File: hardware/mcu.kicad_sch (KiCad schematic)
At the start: 55 parts, among them J10 PRPC001DAAN-RC, J11 PRPC006SAAN-RC, J12 PRPC004SAAN-RC, J8 SBH11-NBPC-D05-SM-BK, J9 PRPC006SAAN-RC, U5 AT25SF081B-SSHD-B, U6 MCP9808, U7 STM32L552CETx, Y1 ABS05-32.768KHZ-9-T, Y2 ECS-160-9-37-CKM-TR3

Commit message: HW: Layout power section
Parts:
- C10, C15, C17, C20: Digi-Key Part Number 732-7902-1-ND -> 732-7623-1-ND; Manufacturer Part Number 885012106005 -> 885012107013
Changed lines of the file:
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@@
 			)
 		)
-		(property "Manufacturer Part Number" "885012106005"
+		(property "Manufacturer Part Number" "885012107013"
 			(at 162.56 33.02 0)
 			(effects
@@
 			)
 		)
-		(property "Digi-Key Part Number" "732-7902-1-ND"
+		(property "Digi-Key Part Number" "732-7623-1-ND"
 			(at 162.56 33.02 0)
 			(effects
@@
 			)
 		)
-		(property "Manufacturer Part Number" "885012106005"
+		(property "Manufacturer Part Number" "885012107013"
 			(at 114.3 166.37 0)
 			(effects
@@
 			)
 		)
-		(property "Digi-Key Part Number" "732-7902-1-ND"
+		(property "Digi-Key Part Number" "732-7623-1-ND"
 			(at 114.3 166.37 0)
 			(effects
@@
 			)
 		)
-		(property "Manufacturer Part Number" "885012106005"
+		(property "Manufacturer Part Number" "885012107013"
 			(at 99.06 33.02 0)
 			(effects
@@
 			)
 		)
-		(property "Digi-Key Part Number" "732-7902-1-ND"
+		(property "Digi-Key Part Number" "732-7623-1-ND"
 			(at 99.06 33.02 0)
 			(effects
@@
 			)
 		)
-		(property "Manufacturer Part Number" "885012106005"
+		(property "Manufacturer Part Number" "885012107013"
 			(at 60.96 168.91 0)
 			(effects
@@
 			)
 		)
-		(property "Digi-Key Part Number" "732-7902-1-ND"
+		(property "Digi-Key Part Number" "732-7623-1-ND"
 			(at 60.96 168.91 0)
 			(effects

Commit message: HW: Layout MCU section
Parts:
- TVS10, TVS11, TVS2, TVS3, TVS4, TVS5, TVS6, TVS7, TVS8, TVS9: value SMAJ6.0CA-13-F -> CPDUC5V0USP-HF; footprint Diode_SMD:D_SMA_Handsoldering -> Diode_SMD:D_0603_1608Metric_Pad1.05x0.95mm_HandSolder; Digi-Key Part Number SMAJ6.0CA-13-FDICT-ND -> 641-1765-1-ND; Manufacturer Diodes Incorporated -> Comchip Technology; Manufacturer Part Number SMAJ6.0CA-13-F -> CPDUC5V0USP-HF
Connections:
- net COM_UART_RX: now also J9.4 (Pin_4), TVS5.1 (K); no longer J9.5 (Pin_5), TVS2.1 (K)
- net COM_UART_TX: now also J9.5 (Pin_5), TVS2.1 (K); no longer J9.4 (Pin_4), TVS5.1 (K)
- net I2C_SCL: now also J12.3 (Pin_3), TVS4.1 (K); no longer J12.2 (Pin_2), TVS7.1 (K)
- net I2C_SDA: now also J12.2 (Pin_2), TVS7.1 (K); no longer J12.3 (Pin_3), TVS4.1 (K)
- net MODEM_RX: now also J11.4 (Pin_4), TVS6.1 (K); no longer J11.5 (Pin_5), TVS3.1 (K)
- net MODEM_TX: now also J11.5 (Pin_5), TVS3.1 (K); no longer J11.4 (Pin_4), TVS6.1 (K)
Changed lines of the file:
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@@
 	(wire
 		(pts
-			(xy 271.78 59.69) (xy 271.78 58.42)
-		)
-		(stroke
-			(width 0)
-			(type default)
-		)
-	)
-	(wire
-		(pts
 			(xy 254 105.41) (xy 262.89 105.41)
 		)
@@
 	(wire
 		(pts
-			(xy 262.89 59.69) (xy 262.89 58.42)
-		)
-		(stroke
-			(width 0)
-			(type default)
-		)
-	)
-	(wire
-		(pts
 			(xy 280.67 31.75) (xy 274.32 31.75)
 		)
@@
 	)
 	(label "I2C_SCL"
-		(at 261.62 120.65 180)
+		(at 252.73 123.19 180)
 		(fields_autoplaced yes)
 		(effects
@@
 	)
 	(label "COM_UART_TX"
-		(at 260.35 48.26 180)
+		(at 251.46 50.8 180)
 		(fields_autoplaced yes)
 		(effects
@@
 	)
 	(label "I2C_SDA"
-		(at 252.73 123.19 180)
+		(at 261.62 120.65 180)
 		(fields_autoplaced yes)
 		(effects
@@
 	)
 	(label "COM_UART_RX"
-		(at 251.46 50.8 180)
+		(at 260.35 48.26 180)
 		(fields_autoplaced yes)
 		(effects
@@
 	(hierarchical_label "MODEM_TX"
 		(shape bidirectional)
-		(at 260.35 93.98 180)
+		(at 251.46 96.52 180)
 		(fields_autoplaced yes)
 		(effects
@@
 	(hierarchical_label "MODEM_RX"
 		(shape bidirectional)
-		(at 251.46 96.52 180)
+		(at 260.35 93.98 180)
 		(fields_autoplaced yes)
 		(effects
@@
 			)
 		)
-		(property "Value" "SMAJ6.0CA-13-F"
+		(property "Value" "CPDUC5V0USP-HF"
 			(at 261.62 102.87 90)
 			(effects
@@
 			)
 		)
-		(property "Footprint" "Diode_SMD:D_SMA_Handsoldering"
+		(property "Footprint" "Diode_SMD:D_0603_1608Metric_Pad1.05x0.95mm_HandSolder"
 			(at 271.78 101.6 0)
 			(effects
@@
 			)
 		)
-		(property "Digi-Key Part Number" "SMAJ6.0CA-13-FDICT-ND"
+		(property "Digi-Key Part Number" "641-1765-1-ND"
 			(at 271.78 101.6 0)
 			(effects
@@
 			)
 		)
-		(property "Manufacturer" "Diodes Incorporated"
+		(property "Manufacturer" "Comchip Technology"
 			(at 271.78 101.6 0)
 			(effects
@@
 			)
 		)
-		(property "Manufacturer Part Number" "SMAJ6.0CA-13-F"
+		(property "Manufacturer Part Number" "CPDUC5V0USP-HF"
 			(at 271.78 101.6 0)
 			(effects
@@
 			)
 		)
-		(property "Value" "SMAJ6.0CA-13-F"
+		(property "Value" "CPDUC5V0USP-HF"
 			(at 243.84 102.87 90)
 			(effects
@@
 			)
 		)
-		(property "Footprint" "Diode_SMD:D_SMA_Handsoldering"
+		(property "Footprint" "Diode_SMD:D_0603_1608Metric_Pad1.05x0.95mm_HandSolder"
 			(at 254 101.6 0)
 			(effects
@@
 			)
 		)
-		(property "Digi-Key Part Number" "SMAJ6.0CA-13-FDICT-ND"
+		(property "Digi-Key Part Number" "641-1765-1-ND"
 			(at 254 101.6 0)
 			(effects
@@
 			)
 		)
-		(property "Manufacturer" "Diodes Incorporated"
+		(property "Manufacturer" "Comchip Technology"
 			(at 254 101.6 0)
 			(effects
@@
 			)
 		)
-		(property "Manufacturer Part Number" "SMAJ6.0CA-13-F"
+		(property "Manufacturer Part Number" "CPDUC5V0USP-HF"
 			(at 254 101.6 0)
 			(effects
@@
 			)
 		)
-		(property "Value" "SMAJ6.0CA-13-F"
+		(property "Value" "CPDUC5V0USP-HF"
 			(at 261.62 74.93 90)
 			(effects
@@
 			)
 		)
-		(property "Footprint" "Diode_SMD:D_SMA_Handsoldering"
+		(property "Footprint" "Diode_SMD:D_0603_1608Metric_Pad1.05x0.95mm_HandSolder"
 			(at 271.78 73.66 0)
 			(effects
@@
 			)
 		)
-		(property "Digi-Key Part Number" "SMAJ6.0CA-13-FDICT-ND"
+		(property "Digi-Key Part Number" "641-1765-1-ND"
 			(at 271.78 73.66 0)
 			(effects
@@
 			)
 		)
-		(property "Manufacturer" "Diodes Incorporated"
+		(property "Manufacturer" "Comchip Technology"
 			(at 271.78 73.66 0)
 			(effects
@@
 			)
 		)
-		(property "Manufacturer Part Number" "SMAJ6.0CA-13-F"
+		(property "Manufacturer Part Number" "CPDUC5V0USP-HF"
 			(at 271.78 73.66 0)
 			(effects
@@
 			)
 		)
-		(property "Value" "SMAJ6.0CA-13-F"
+		(property "Value" "CPDUC5V0USP-HF"
 			(at 252.73 102.87 90)
 			(effects
@@
 			)
 		)
-		(property "Footprint" "Diode_SMD:D_SMA_Handsoldering"
+		(property "Footprint" "Diode_SMD:D_0603_1608Metric_Pad1.05x0.95mm_HandSolder"
 			(at 262.89 101.6 0)
 			(effects
@@
 			)
 		)
-		(property "Digi-Key Part Number" "SMAJ6.0CA-13-FDICT-ND"
+		(property "Digi-Key Part Number" "641-1765-1-ND"
 			(at 262.89 101.6 0)
 			(effects
@@
 			)
 		)
-		(property "Manufacturer" "Diodes Incorporated"
+		(property "Manufacturer" "Comchip Technology"
 			(at 262.89 101.6 0)
 			(effects
@@
 			)
 		)
-		(property "Manufacturer Part Number" "SMAJ6.0CA-13-F"
+		(property "Manufacturer Part Number" "CPDUC5V0USP-HF"
 			(at 262.89 101.6 0)
 			(effects
@@
 			)
 		)
-		(property "Value" "SMAJ6.0CA-13-F"
+		(property "Value" "CPDUC5V0USP-HF"
 			(at 252.73 57.15 90)
 			(effects
@@
 			)
 		)
-		(property "Footprint" "Diode_SMD:D_SMA_Handsoldering"
+		(property "Footprint" "Diode_SMD:D_0603_1608Metric_Pad1.05x0.95mm_HandSolder"
 			(at 262.89 55.88 0)
 			(effects
@@
 			)
 		)
-		(property "Digi-Key Part Number" "SMAJ6.0CA-13-FDICT-ND"
+		(property "Digi-Key Part Number" "641-1765-1-ND"
 			(at 262.89 55.88 0)
 			(effects
@@
 			)
 		)
-		(property "Manufacturer" "Diodes Incorporated"
+		(property "Manufacturer" "Comchip Technology"
 			(at 262.89 55.88 0)
 			(effects
@@
 			)
 		)
-		(property "Manufacturer Part Number" "SMAJ6.0CA-13-F"
+		(property "Manufacturer Part Number" "CPDUC5V0USP-HF"
 			(at 262.89 55.88 0)
 			(effects
@@
 			)
 		)
-		(property "Value" "SMAJ6.0CA-13-F"
+		(property "Value" "CPDUC5V0USP-HF"
 			(at 261.62 57.15 90)
 			(effects
@@
 			)
 		)
-		(property "Footprint" "Diode_SMD:D_SMA_Handsoldering"
+		(property "Footprint" "Diode_SMD:D_0603_1608Metric_Pad1.05x0.95mm_HandSolder"
 			(at 271.78 55.88 0)
 			(effects
@@
 			)
 		)
-		(property "Digi-Key Part Number" "SMAJ6.0CA-13-FDICT-ND"
+		(property "Digi-Key Part Number" "641-1765-1-ND"
 			(at 271.78 55.88 0)
 			(effects
@@
 			)
 		)
-		(property "Manufacturer" "Diodes Incorporated"
+		(property "Manufacturer" "Comchip Technology"
 			(at 271.78 55.88 0)
 			(effects
@@
 			)
 		)
-		(property "Manufacturer Part Number" "SMAJ6.0CA-13-F"
+		(property "Manufacturer Part Number" "CPDUC5V0USP-HF"
 			(at 271.78 55.88 0)
 			(effects
@@
 			)
 		)
-		(property "Value" "SMAJ6.0CA-13-F"
+		(property "Value" "CPDUC5V0USP-HF"
 			(at 243.84 129.54 90)
 			(effects
@@
 			)
 		)
-		(property "Footprint" "Diode_SMD:D_SMA_Handsoldering"
+		(property "Footprint" "Diode_SMD:D_0603_1608Metric_Pad1.05x0.95mm_HandSolder"
 			(at 254 128.27 0)
 			(effects
@@
 			)
 		)
-		(property "Digi-Key Part Number" "SMAJ6.0CA-13-FDICT-ND"
+		(property "Digi-Key Part Number" "641-1765-1-ND"
 			(at 254 128.27 0)
 			(effects
@@
 			)
 		)
-		(property "Manufacturer" "Diodes Incorporated"
+		(property "Manufacturer" "Comchip Technology"
 			(at 254 128.27 0)
 			(effects
@@
 			)
 		)
-		(property "Manufacturer Part Number" "SMAJ6.0CA-13-F"
+		(property "Manufacturer Part Number" "CPDUC5V0USP-HF"
 			(at 254 128.27 0)
 			(effects
@@
 			)
 		)
-		(property "Value" "SMAJ6.0CA-13-F"
+		(property "Value" "CPDUC5V0USP-HF"
 			(at 243.84 57.15 90)
 			(effects
@@
 			)
 		)
-		(property "Footprint" "Diode_SMD:D_SMA_Handsoldering"
+		(property "Footprint" "Diode_SMD:D_0603_1608Metric_Pad1.05x0.95mm_HandSolder"
 			(at 254 55.88 0)
 			(effects
@@
 			)
 		)
-		(property "Digi-Key Part Number" "SMAJ6.0CA-13-FDICT-ND"
+		(property "Digi-Key Part Number" "641-1765-1-ND"
 			(at 254 55.88 0)
 			(effects
@@
 			)
 		)
-		(property "Manufacturer" "Diodes Incorporated"
+		(property "Manufacturer" "Comchip Technology"
 			(at 254 55.88 0)
 			(effects
@@
 			)
 		)
-		(property "Manufacturer Part Number" "SMAJ6.0CA-13-F"
+		(property "Manufacturer Part Number" "CPDUC5V0USP-HF"
 			(at 254 55.88 0)
 			(effects
@@
 			)
 		)
-		(property "Value" "SMAJ6.0CA-13-F"
+		(property "Value" "CPDUC5V0USP-HF"
 			(at 252.73 129.54 90)
 			(effects
@@
 			)
 		)
-		(property "Footprint" "Diode_SMD:D_SMA_Handsoldering"
+		(property "Footprint" "Diode_SMD:D_0603_1608Metric_Pad1.05x0.95mm_HandSolder"
 			(at 262.89 128.27 0)
 			(effects
@@
 			)
 		)
-		(property "Digi-Key Part Number" "SMAJ6.0CA-13-FDICT-ND"
+		(property "Digi-Key Part Number" "641-1765-1-ND"
 			(at 262.89 128.27 0)
 			(effects
@@
 			)
 		)
-		(property "Manufacturer" "Diodes Incorporated"
+		(property "Manufacturer" "Comchip Technology"
 			(at 262.89 128.27 0)
 			(effects
@@
 			)
 		)
-		(property "Manufacturer Part Number" "SMAJ6.0CA-13-F"
+		(property "Manufacturer Part Number" "CPDUC5V0USP-HF"
 			(at 262.89 128.27 0)
 			(effects
@@
 			)
 		)
-		(property "Value" "SMAJ6.0CA-13-F"
+		(property "Value" "CPDUC5V0USP-HF"
 			(at 261.62 129.54 90)
 			(effects
@@
 			)
 		)
-		(property "Footprint" "Diode_SMD:D_SMA_Handsoldering"
+		(property "Footprint" "Diode_SMD:D_0603_1608Metric_Pad1.05x0.95mm_HandSolder"
 			(at 271.78 128.27 0)
 			(effects
@@
 			)
 		)
-		(property "Digi-Key Part Number" "SMAJ6.0CA-13-FDICT-ND"
+		(property "Digi-Key Part Number" "641-1765-1-ND"
 			(at 271.78 128.27 0)
 			(effects
@@
 			)
 		)
-		(property "Manufacturer" "Diodes Incorporated"
+		(property "Manufacturer" "Comchip Technology"
 			(at 271.78 128.27 0)
 			(effects
@@
 			)
 		)
-		(property "Manufacturer Part Number" "SMAJ6.0CA-13-F"
+		(property "Manufacturer Part Number" "CPDUC5V0USP-HF"
 			(at 271.78 128.27 0)
 			(effects

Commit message: HW: Fix programming header and layout
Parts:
- J8: footprint Connector_PinHeader_2.54mm:PinHeader_2x05_P2.54mm_Vertical_SMD -> Connector_IDC:IDC-Header_2x05_P2.54mm_Vertical_SMD
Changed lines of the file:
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@@
 			)
 		)
-		(property "Footprint" "Connector_PinHeader_2.54mm:PinHeader_2x05_P2.54mm_Vertical_SMD"
+		(property "Footprint" "Connector_IDC:IDC-Header_2x05_P2.54mm_Vertical_SMD"
 			(at 265.43 152.4 0)
 			(effects

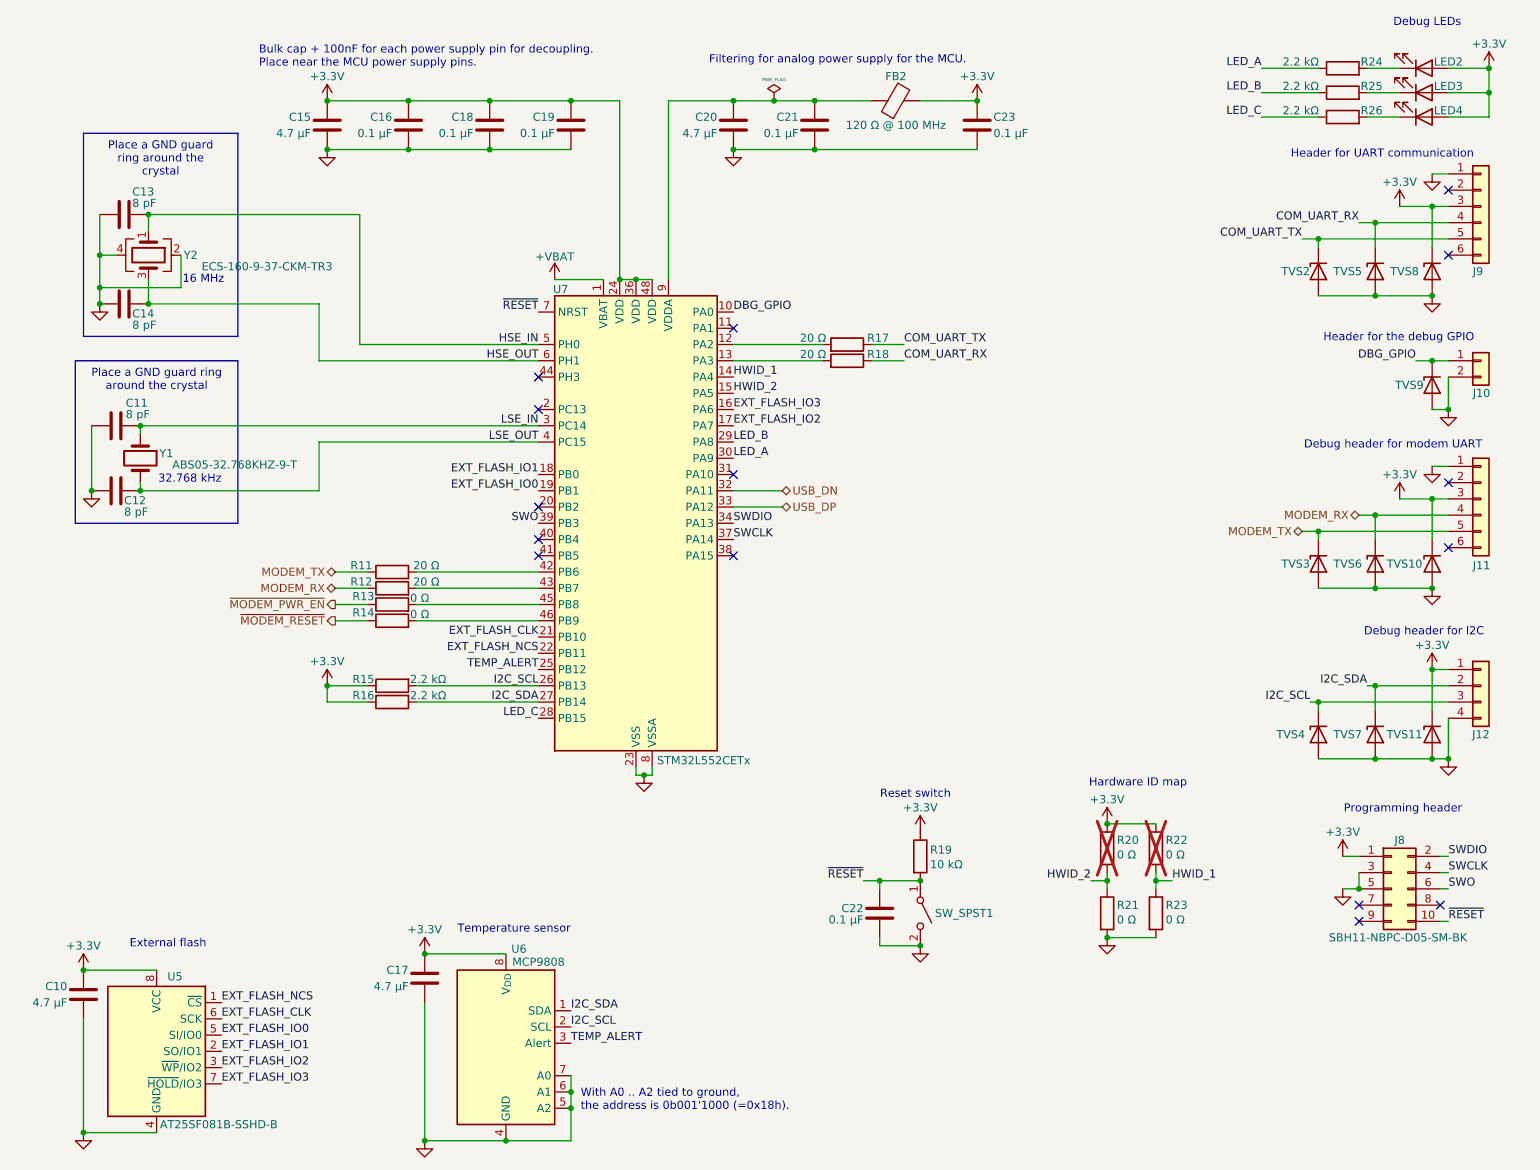
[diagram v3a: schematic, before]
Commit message: HW: Add bulk cap to VBAT
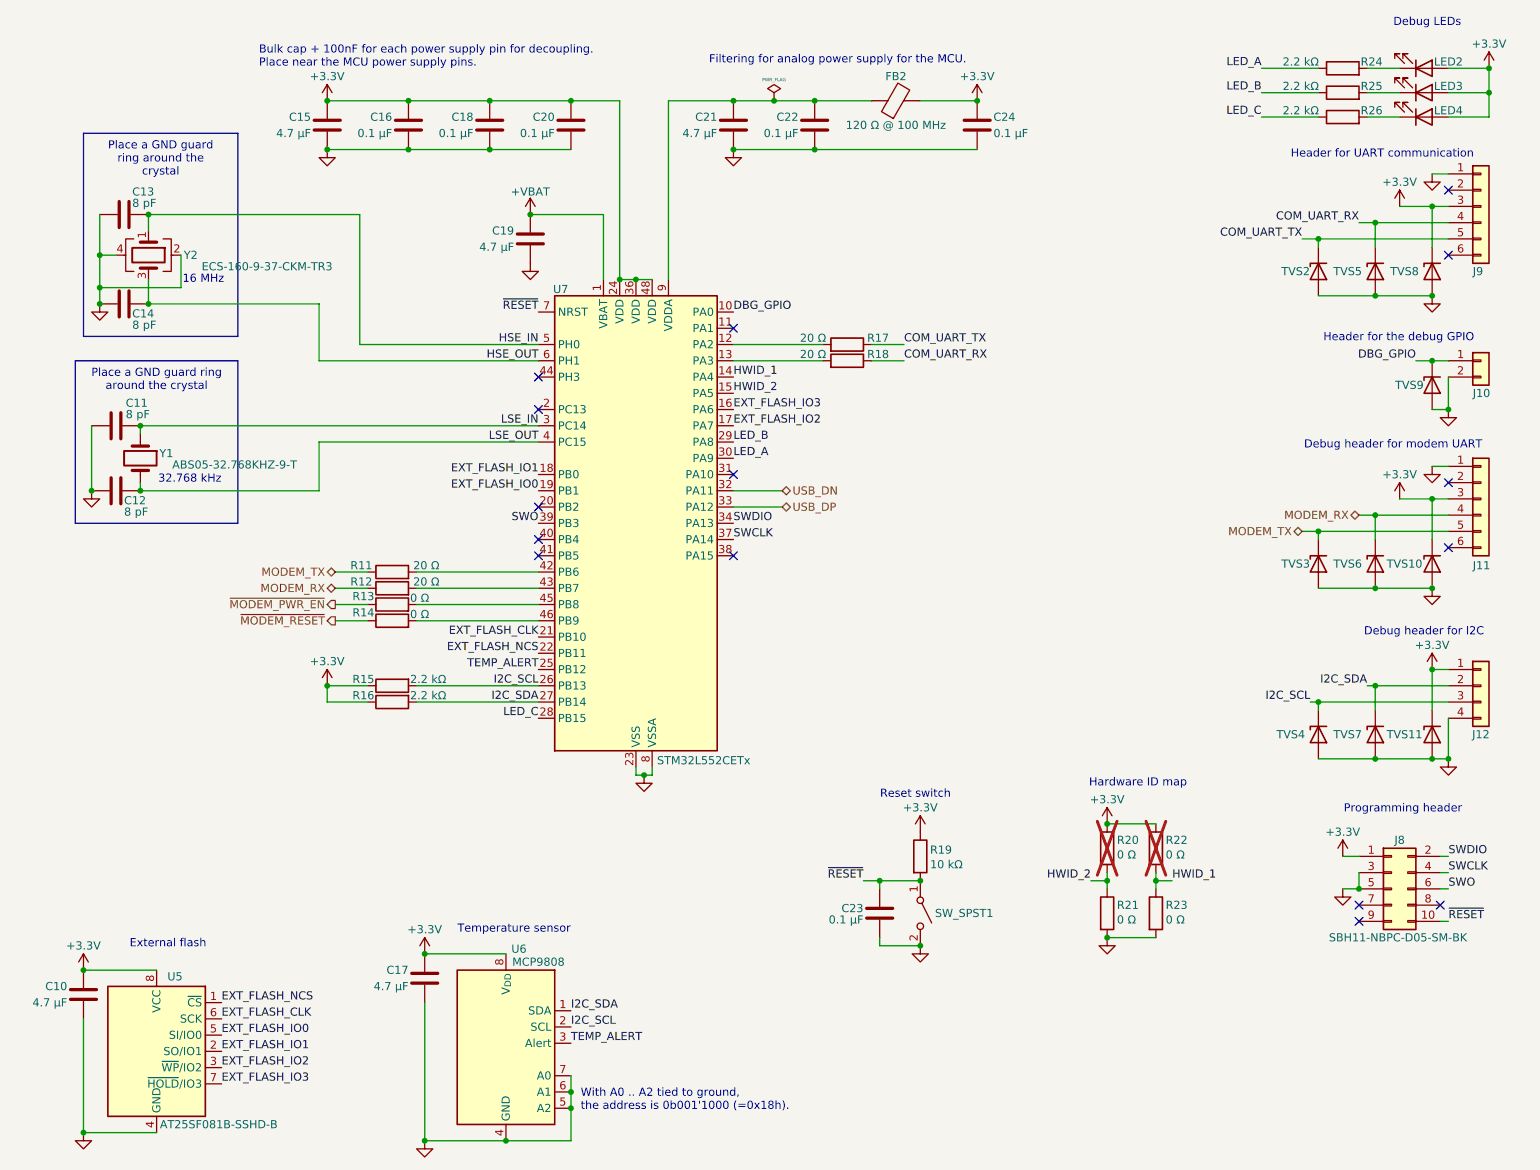
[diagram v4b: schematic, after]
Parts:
- added C19: 4.7 µF, Capacitor_SMD:C_0603_1608Metric_Pad1.08x0.95mm_HandSolder, symbol Device:C
- renumbered C19 to C20, C20 to C21, C21 to C22, C22 to C23, C23 to C24
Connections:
- net +VBAT: now also C19.1
- net GND: now also C19.2

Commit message: HW: Refine schema
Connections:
- net EXT_FLASH_CLK renamed EXT_FLASH_SCK
- net EXT_FLASH_NCS renamed EXT_FLASH_~{CS}
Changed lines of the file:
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@@
-		)
-	)
-	(label "EXT_FLASH_NCS"
-		(at 132.08 115.57 180)
-		(fields_autoplaced yes)
-		(effects
-			(font
-				(size 1.27 1.27)
-			)
-			(justify right bottom)
 		)
 	)
@@
 		)
 	)
+	(label "EXT_FLASH_~{CS}"
+		(at 132.08 115.57 180)
+		(fields_autoplaced yes)
+		(effects
+			(font
+				(size 1.27 1.27)
+			)
+			(justify right bottom)
+		)
+	)
 	(label "I2C_SCL"
 		(at 252.73 123.19 180)
@@
 		)
 	)
-	(label "EXT_FLASH_CLK"
+	(label "EXT_FLASH_SCK"
 		(at 132.08 113.03 180)
 		(fields_autoplaced yes)
@@
 		)
 	)
-	(label "EXT_FLASH_NCS"
+	(label "EXT_FLASH_~{CS}"
 		(at 82.55 170.18 0)
 		(fields_autoplaced yes)
@@
 		)
 	)
-	(label "EXT_FLASH_CLK"
+	(label "EXT_FLASH_SCK"
 		(at 82.55 172.72 0)
 		(fields_autoplaced yes)

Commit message: HW: Update components
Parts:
- SW_SPST1: value PTS645SK50SMTR92 LFS -> 430182050816; Digi-Key Part Number CKN9087CT-ND -> 732-7005-1-ND; Manufacturer C&K -> Würth Elektronik; Manufacturer Part Number PTS645SK50SMTR92 LFS -> 430182050816
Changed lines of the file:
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@@
 			)
 		)
-		(property "Value" "PTS645SK50SMTR92 LFS"
+		(property "Value" "430182050816"
 			(at 187.198 157.988 90)
 			(effects
@@
 			)
 		)
-		(property "Manufacturer" "C&K"
+		(property "Manufacturer" "Würth Elektronik"
 			(at 191.77 156.21 90)
 			(effects
@@
 			)
 		)
-		(property "Manufacturer Part Number" "PTS645SK50SMTR92 LFS"
+		(property "Manufacturer Part Number" "430182050816"
 			(at 191.77 156.21 90)
 			(effects
@@
 			)
 		)
-		(property "Digi-Key Part Number" "CKN9087CT-ND"
+		(property "Digi-Key Part Number" "732-7005-1-ND"
 			(at 191.77 156.21 90)
 			(effects
